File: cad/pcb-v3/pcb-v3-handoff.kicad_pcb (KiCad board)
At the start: 4 copper layers, 19.3 x 19.3 mm, 46 parts

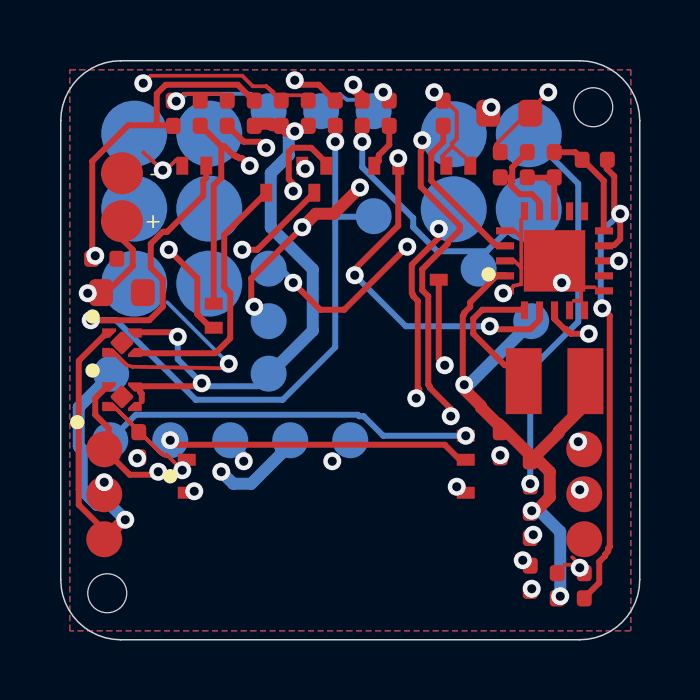
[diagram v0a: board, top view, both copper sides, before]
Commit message: KiCad 10 changed the file format and my parsers went blind
Filling the zones round-tripped the board through KiCad 10, which writes a NEW
format: the top-level (net N "NAME") table is GONE and every item now carries
(net "NAME") directly. sexp.pads() read index [2] and returned 134 pads with
ZERO nets. A checker that sees no nets passes everything -- the most dangerous
possible failure, and it would have reported a clean board.

(KRT's own checkers were fine: they print 'Checking 27 routed nets'.)

Fixed sexp.net_of()/net_table() and every preflight pattern to accept BOTH
formats, then re-ran and found two things the blind version had hidden:

REAL: a GND tap via at (-5.20, 4.70) put 0.05mm of copper inside the ANTENNA
keep-out. gnd_taps excluded via CENTRES inside a keep-out but never grew it by
the via's own radius -- a keep-out applies to copper, not to a centre point.
Now dilated by VIA_D/2 + clearance; taps redone; zero intrusions.

FALSE: check 7 reported all three pours inside the keep-out. KiCad writes a
filled zone as one KEYHOLED ring (into each hole and back along a zero-width
slit), so the raw ring is self-intersecting and INVALID, and .intersects() on
invalid geometry answers nonsense. Repaired with buffer(0) and switched to an
AREA test: true overlap 0.000000 mm2. Boundary contact is not intrusion.
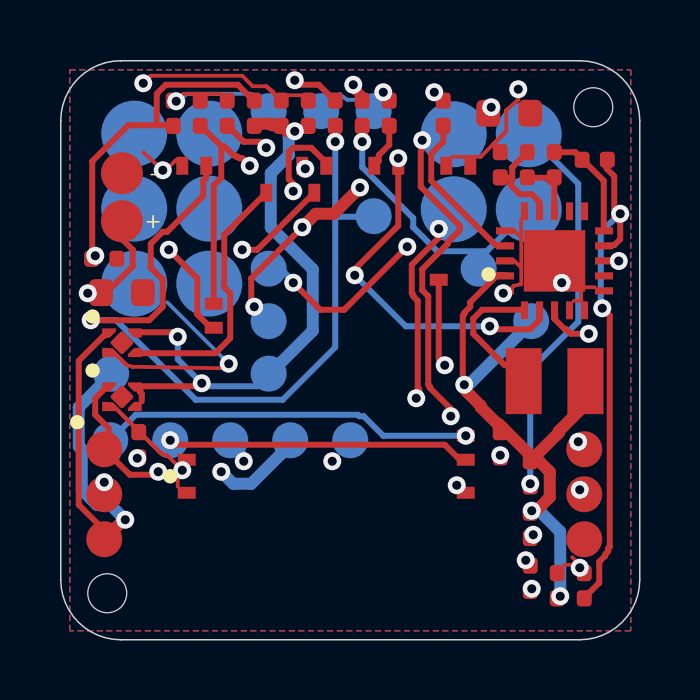
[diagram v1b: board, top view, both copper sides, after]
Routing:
- net GND: track 38.0 -> 37.2 mm, vias 15 -> 14
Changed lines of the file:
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@@
 	(segment (start -2.5000 -8.5000) (end -2.8000 -8.8000) (width 0.127) (layer "F.Cu") (net 3))
 	(segment (start -4.3500 -8.5500) (end -5.2500 -8.5500) (width 0.127) (layer "F.Cu") (net 3))
-	(segment (start 6.3500 -8.3500) (end 6.6000 -8.6000) (width 0.127) (layer "F.Cu") (net 3))
+	(segment (start 5.6000 -8.3500) (end 5.6000 -8.7000) (width 0.127) (layer "F.Cu") (net 3))
 	(segment (start -6.8000 2.9500) (end -6.3500 3.4000) (width 0.127) (layer "F.Cu") (net 3))
 	(segment (start -6.3500 3.4000) (end -6.2000 3.5000) (width 0.127) (layer "F.Cu") (net 3))
@@
 	(segment (start -0.6000 3.6000) (end -0.6000 3.7000) (width 0.127) (layer "B.Cu") (net 3))
 	(segment (start -6.1000 -1.6000) (end -4.0500 0.4500) (width 0.127) (layer "B.Cu") (net 3))
-	(segment (start 4.8500 -6.8500) (end 6.3500 -8.3500) (width 0.127) (layer "F.Cu") (net 3))
+	(segment (start 4.7500 -6.8500) (end 5.2000 -7.3000) (width 0.127) (layer "F.Cu") (net 3))
+	(segment (start 5.2000 -7.3000) (end 5.2000 -8.0000) (width 0.127) (layer "F.Cu") (net 3))
+	(segment (start 5.2000 -8.0000) (end 5.6000 -8.3500) (width 0.127) (layer "F.Cu") (net 3))
 	(segment (start -3.3000 -8.5500) (end -5.4500 -8.5500) (width 0.127) (layer "B.Cu") (net 3))
 	(segment (start -5.4500 -8.5500) (end -5.6000 -8.4000) (width 0.127) (layer "B.Cu") (net 3))
@@
 	(segment (start -0.1000 -8.3500) (end 0.7500 -8.3500) (width 0.127) (layer "B.Cu") (net 3))
 	(segment (start 0.7500 -8.3500) (end 0.9000 -8.5000) (width 0.127) (layer "B.Cu") (net 3))
+	(segment (start -5.7500 4.5500) (end -5.7500 4.2500) (width 0.127) (layer "F.Cu") (net 3))
 	(segment (start -5.8000 -6.3500) (end -6.0500 -6.1000) (width 0.127) (layer "F.Cu") (net 3))
-	(segment (start 3.0500 -6.4500) (end 3.4000 -6.8000) (width 0.127) (layer "F.Cu") (net 3))
-	(segment (start 3.4000 -6.8000) (end 3.4000 -6.9000) (width 0.127) (layer "F.Cu") (net 3))
-	(segment (start 3.4000 -6.9000) (end 3.5500 -7.0500) (width 0.127) (layer "F.Cu") (net 3))
-	(segment (start 3.5500 -7.0500) (end 3.5500 -7.9500) (width 0.127) (layer "F.Cu") (net 3))
-	(segment (start 3.5500 -7.9500) (end 3.0000 -8.5000) (width 0.127) (layer "F.Cu") (net 3))
-	(segment (start 3.8000 -6.4500) (end 3.4000 -6.8000) (width 0.127) (layer "F.Cu") (net 3))
+	(segment (start 3.4000 -6.4500) (end 4.3500 -6.4500) (width 0.127) (layer "F.Cu") (net 3))
+	(segment (start 4.3500 -6.4500) (end 5.2000 -7.3000) (width 0.127) (layer "F.Cu") (net 3))
 	(segment (start 8.1500 -2.1000) (end 7.2000 -2.1000) (width 0.127) (layer "F.Cu") (net 3))
 	(segment (start 7.2000 -2.1000) (end 7.0500 -2.2500) (width 0.127) (layer "F.Cu") (net 3))
@@
 	(via (at -6.2500 -6.0000) (size 0.6) (drill 0.3) (layers "F.Cu" "B.Cu") (net 3))
 	(via (at 7.6500 7.2500) (size 0.6) (drill 0.3) (layers "F.Cu" "B.Cu") (net 3))
-	(via (at 5.7500 7.0000) (size 0.6) (drill 0.3) (layers "F.Cu" "B.Cu") (net 3))
+	(via (at 5.8500 7.0000) (size 0.6) (drill 0.3) (layers "F.Cu" "B.Cu") (net 3))
 	(via (at -5.8000 -8.3000) (size 0.6) (drill 0.3) (layers "F.Cu" "B.Cu") (net 3))
 	(via (at -6.9000 -8.9000) (size 0.6) (drill 0.3) (layers "F.Cu" "B.Cu") (net 3))
 	(via (at 2.8000 -8.6000) (size 0.6) (drill 0.3) (layers "F.Cu" "B.Cu") (net 3))
-	(via (at 6.6000 -8.6000) (size 0.6) (drill 0.3) (layers "F.Cu" "B.Cu") (net 3))
+	(via (at 5.6000 -8.7000) (size 0.6) (drill 0.3) (layers "F.Cu" "B.Cu") (net 3))
 	(via (at -5.6000 4.0000) (size 0.6) (drill 0.3) (layers "F.Cu" "B.Cu") (net 3))
 	(via (at 1.1000 -8.6000) (size 0.6) (drill 0.3) (layers "F.Cu" "B.Cu") (net 3))
 	(via (at -0.6000 3.7000) (size 0.6) (drill 0.3) (layers "F.Cu" "B.Cu") (net 3))
 	(via (at -4.0500 0.4500) (size 0.6) (drill 0.3) (layers "F.Cu" "B.Cu") (net 3))
-	(via (at -5.2000 4.7000) (size 0.6) (drill 0.3) (layers "F.Cu" "B.Cu") (net 3))
-	(via (at 3.5500 4.5500) (size 0.6) (drill 0.3) (layers "F.Cu" "B.Cu") (net 3))
+	(via (at 3.5500 4.5000) (size 0.6) (drill 0.3) (layers "F.Cu" "B.Cu") (net 3))
 	(via (at 5.1000 -1.9000) (size 0.6) (drill 0.3) (layers "F.Cu" "B.Cu") (net 3))
 	(via (at 7.0500 -2.2500) (size 0.6) (drill 0.3) (layers "F.Cu" "B.Cu") (net 3))

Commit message: Zones filled in KiCad 10: 19/19 checks pass, 0 blockers
Verified after the round-trip: parsers still see 124 nets (the KiCad 10 format
trap), stackup 1.2000mm intact, zone_connect x3 and the BT1 mask margin
survived KiCad's save. 3 filled zones - F.Cu 144.53, B.Cu 157.87, In2.Cu
255.80 mm2 - and copper inside the antenna keep-out measures 0.000000 mm2.

Independently confirmed: KRT DRC clean, KRT connectivity 'Checking 27 routed
nets / ALL NETS FULLY CONNECTED'.

Remaining are two judgement calls, not defects: VBAT has no 0.40mm trunk
(0.2mm over 27mm is ~66 milliohm, nothing beside the cell's ESR) and the
J4/J11 pogo pads rest on a measurement only Daniel can confirm.
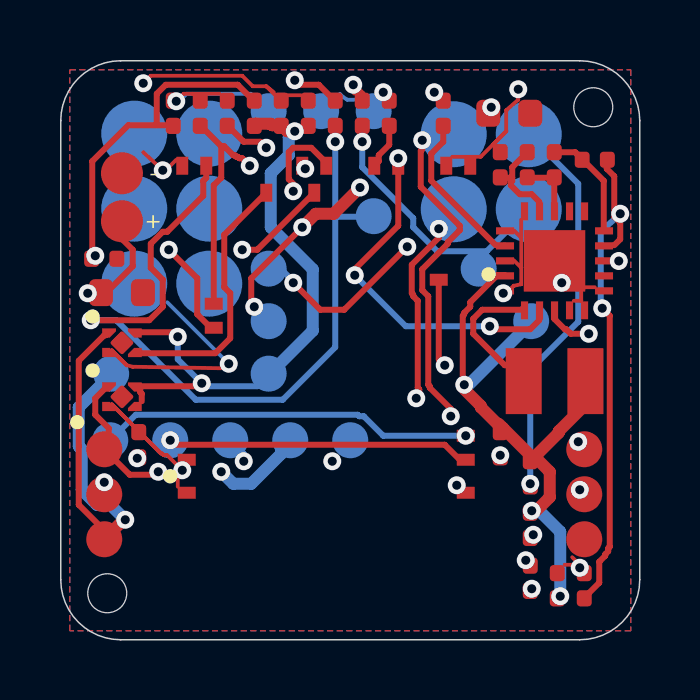
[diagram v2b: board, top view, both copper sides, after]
